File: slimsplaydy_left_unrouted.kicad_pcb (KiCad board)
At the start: 2 copper layers, 122.3 x 94.4 mm, 44 parts

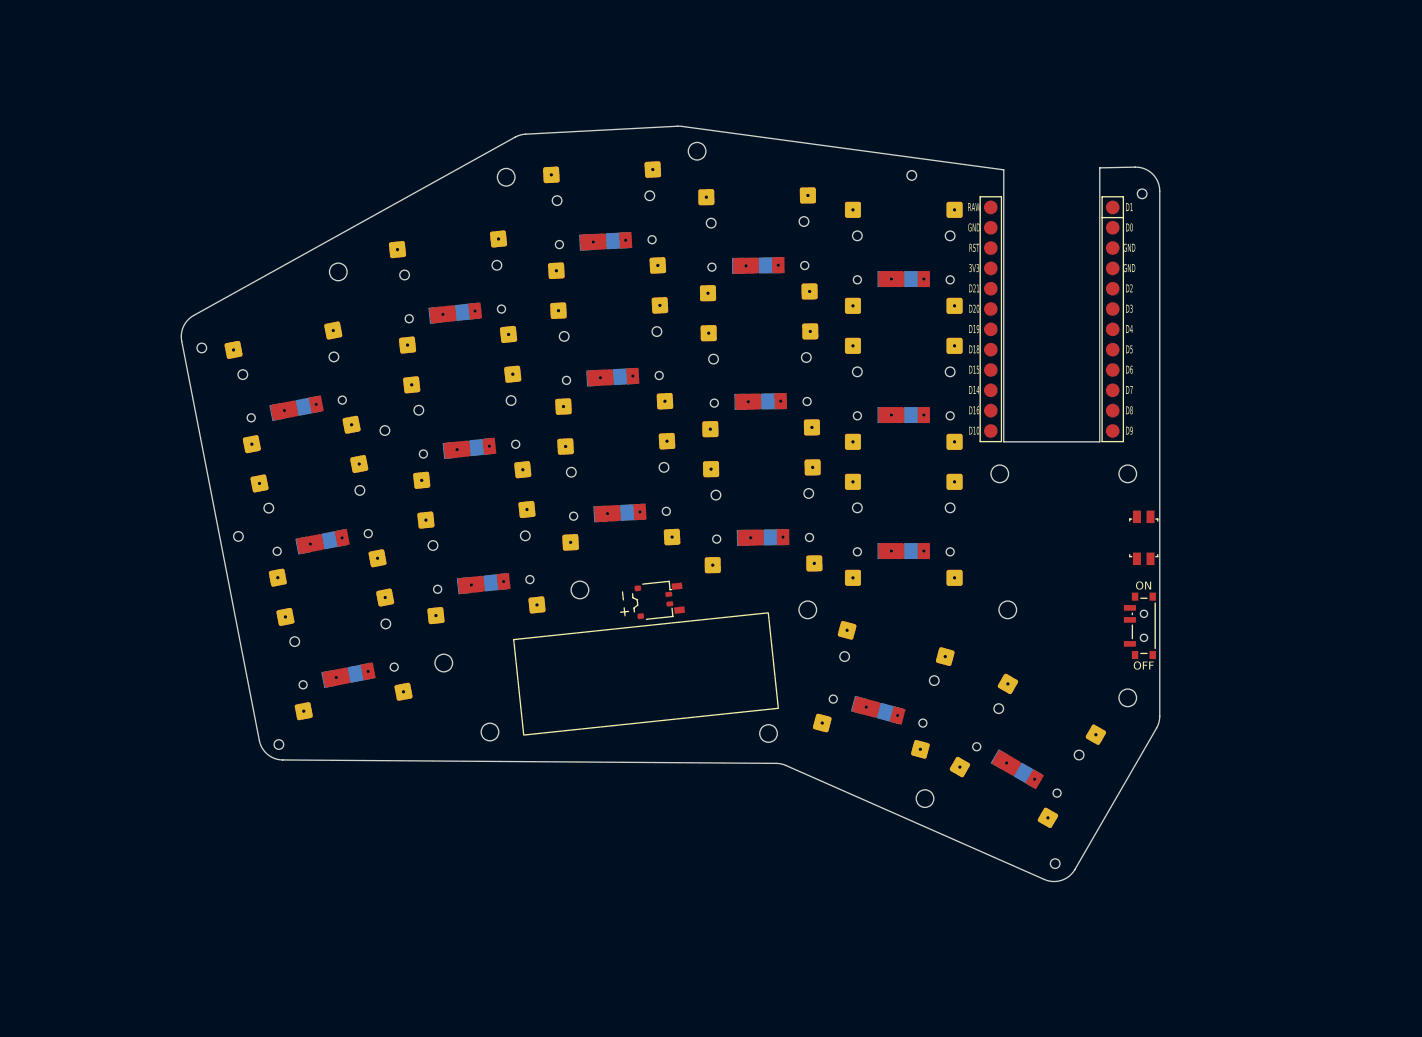
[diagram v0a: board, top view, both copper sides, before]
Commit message: Add via holesize options separate from via size options.
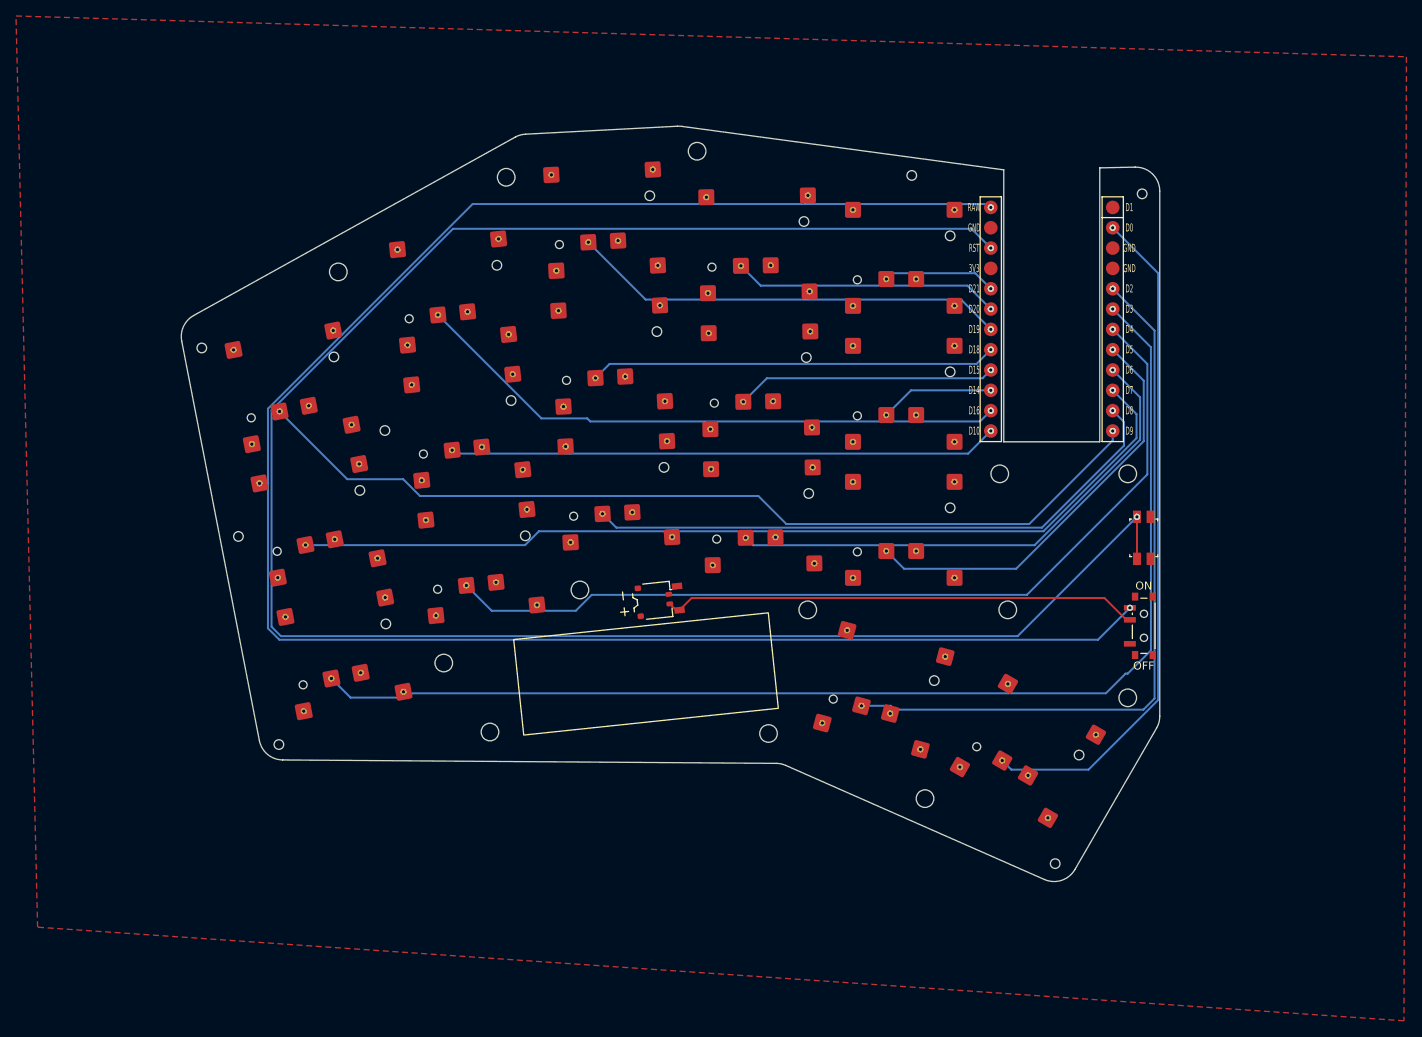
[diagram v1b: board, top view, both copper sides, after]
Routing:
- net RST: track 0.00 -> 247.5 mm, vias 0 -> 2
- net RAW: track 0.00 -> 238.6 mm, vias 0 -> 2
- net hand_pinky_bottom: track 0.00 -> 150.5 mm, vias 0 -> 1
- net hand_pinky_home: track 0.00 -> 116.6 mm, vias 0 -> 1
- net hand_pinky_top: track 0.00 -> 115.5 mm, vias 0 -> 1
- net hand_ring_bottom: track 0.00 -> 113.4 mm, vias 0 -> 1
- net thumb_near_fan: track 0.00 -> 90.8 mm, vias 0 -> 1
- net thumb_far_fan: track 0.00 -> 84.9 mm, vias 0 -> 1
- net hand_ring_top: track 0.00 -> 75.2 mm, vias 0 -> 1
- net hand_middle_bottom: track 0.00 -> 75.1 mm, vias 0 -> 1
- net hand_ring_home: track 0.00 -> 68.7 mm, vias 0 -> 1
- net hand_index_bottom: track 0.00 -> 65.3 mm, vias 0 -> 1
- net BAT_P: track 0.00 -> 59.6 mm
- net hand_middle_top: track 0.00 -> 54.8 mm, vias 0 -> 1
- net hand_inner_bottom: track 0.00 -> 52.7 mm, vias 0 -> 1
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- added copper zone on F.Cu, net GND
